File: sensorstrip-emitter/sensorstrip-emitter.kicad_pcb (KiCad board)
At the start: 2 copper layers, 40 x 12.5 mm, 8 parts, among them J1 Conn_01x02_MountingPin, J2 Conn_01x02_MountingPin

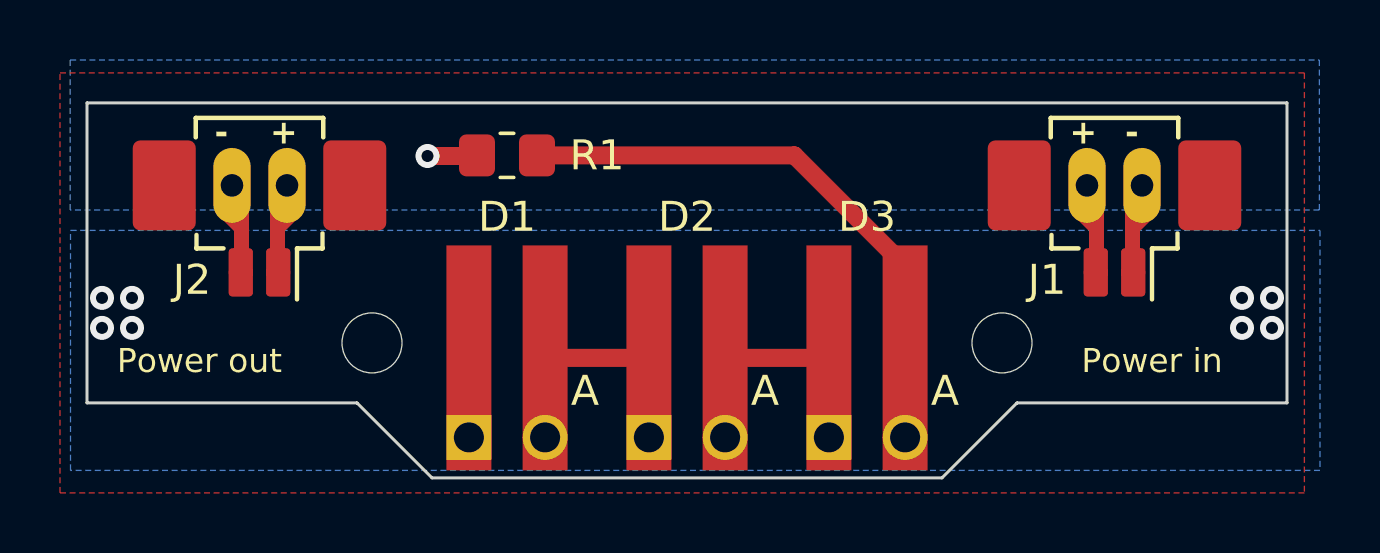
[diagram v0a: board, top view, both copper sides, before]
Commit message: Rename sender / receiver boards to power-emitter and emitter
...hopefully this is clearer

Also some tidying of older boards
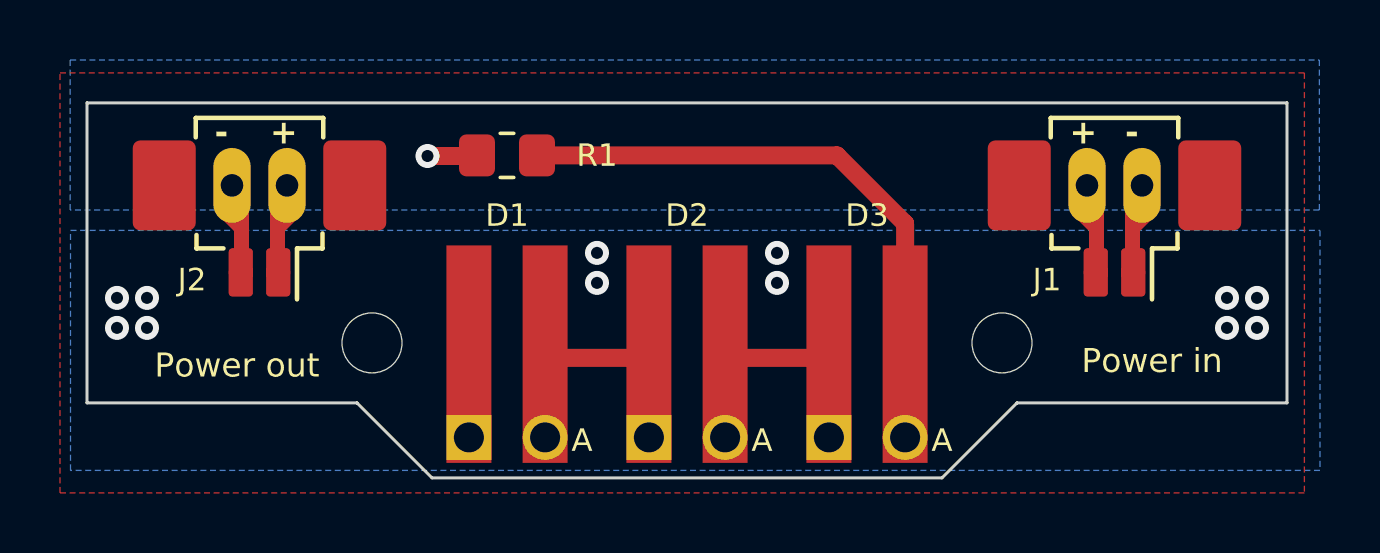
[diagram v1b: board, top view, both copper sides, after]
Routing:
- net /D3+: track 13.8 -> 17.7 mm
- net GND: vias 8 -> 12
